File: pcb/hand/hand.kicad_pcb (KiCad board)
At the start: 2 copper layers, 172.5 x 135.2 mm, 48 parts, among them J1 Conn_01x15, J2 Conn_01x15

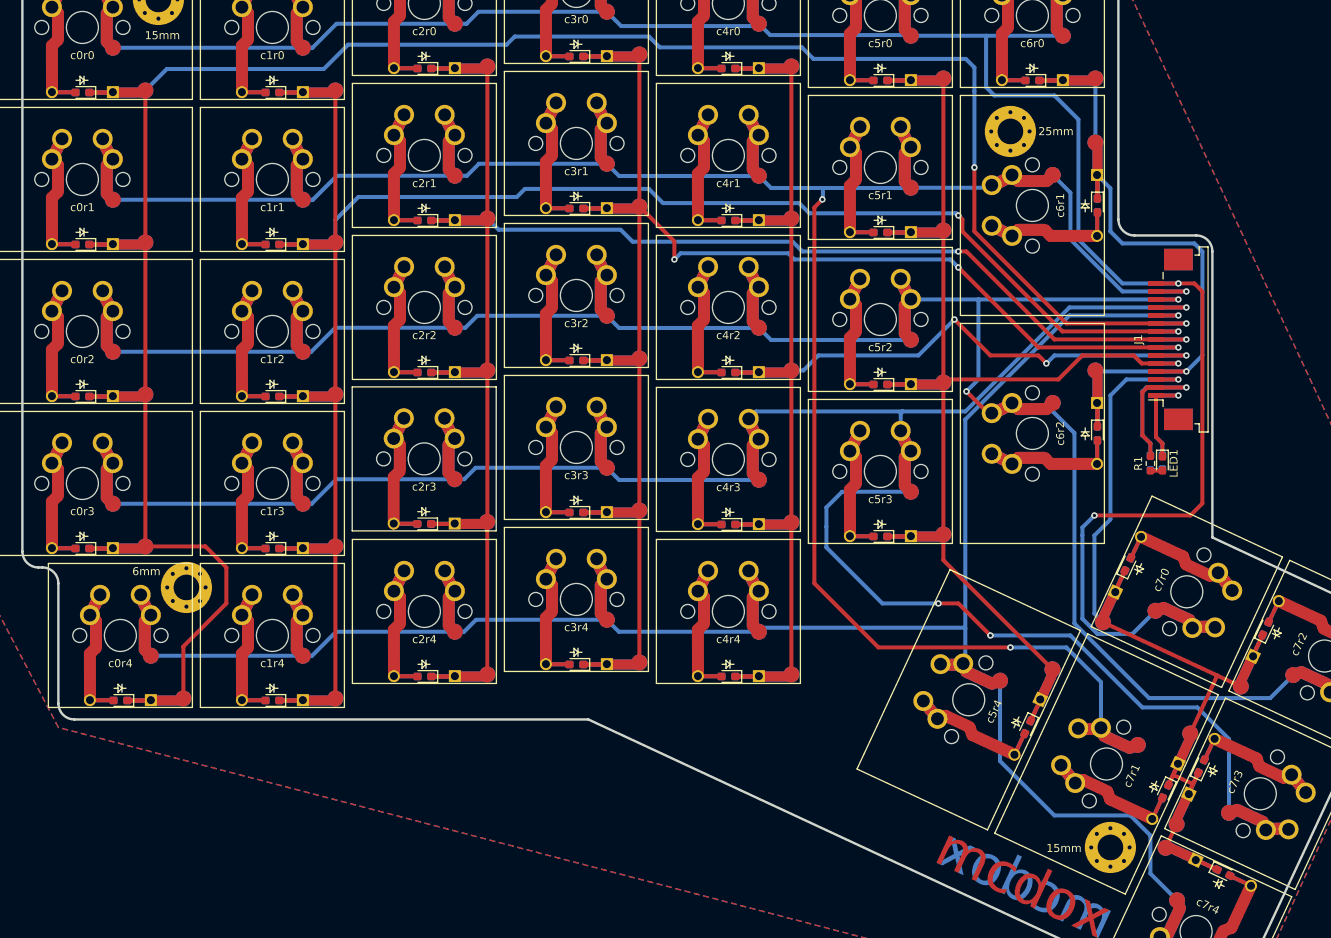
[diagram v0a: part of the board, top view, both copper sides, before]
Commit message: pcb/hand SOD123 diodes
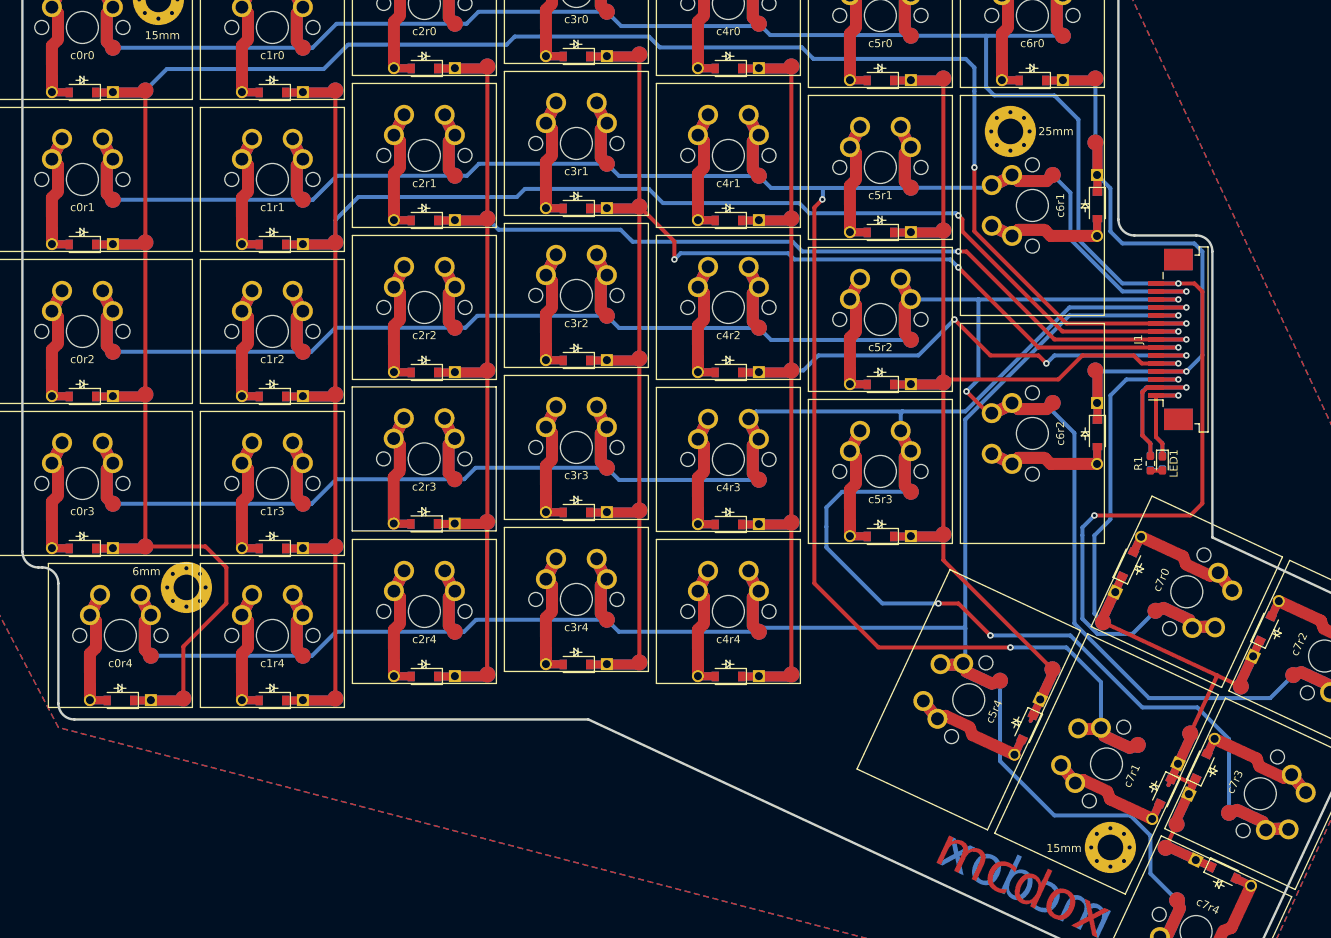
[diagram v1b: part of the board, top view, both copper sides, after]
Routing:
- net col7: track 145.9 -> 137.6 mm
- net col0: track 321.4 -> 313.4 mm
- net col2: track 244.5 -> 238.5 mm
- net col4: track 205.6 -> 199.6 mm
- net col3: track 226.5 -> 220.5 mm
- net col1: track 267.9 -> 261.9 mm
- net col6: track 102.0 -> 96.8 mm
- net col5: track 184.5 -> 179.7 mm

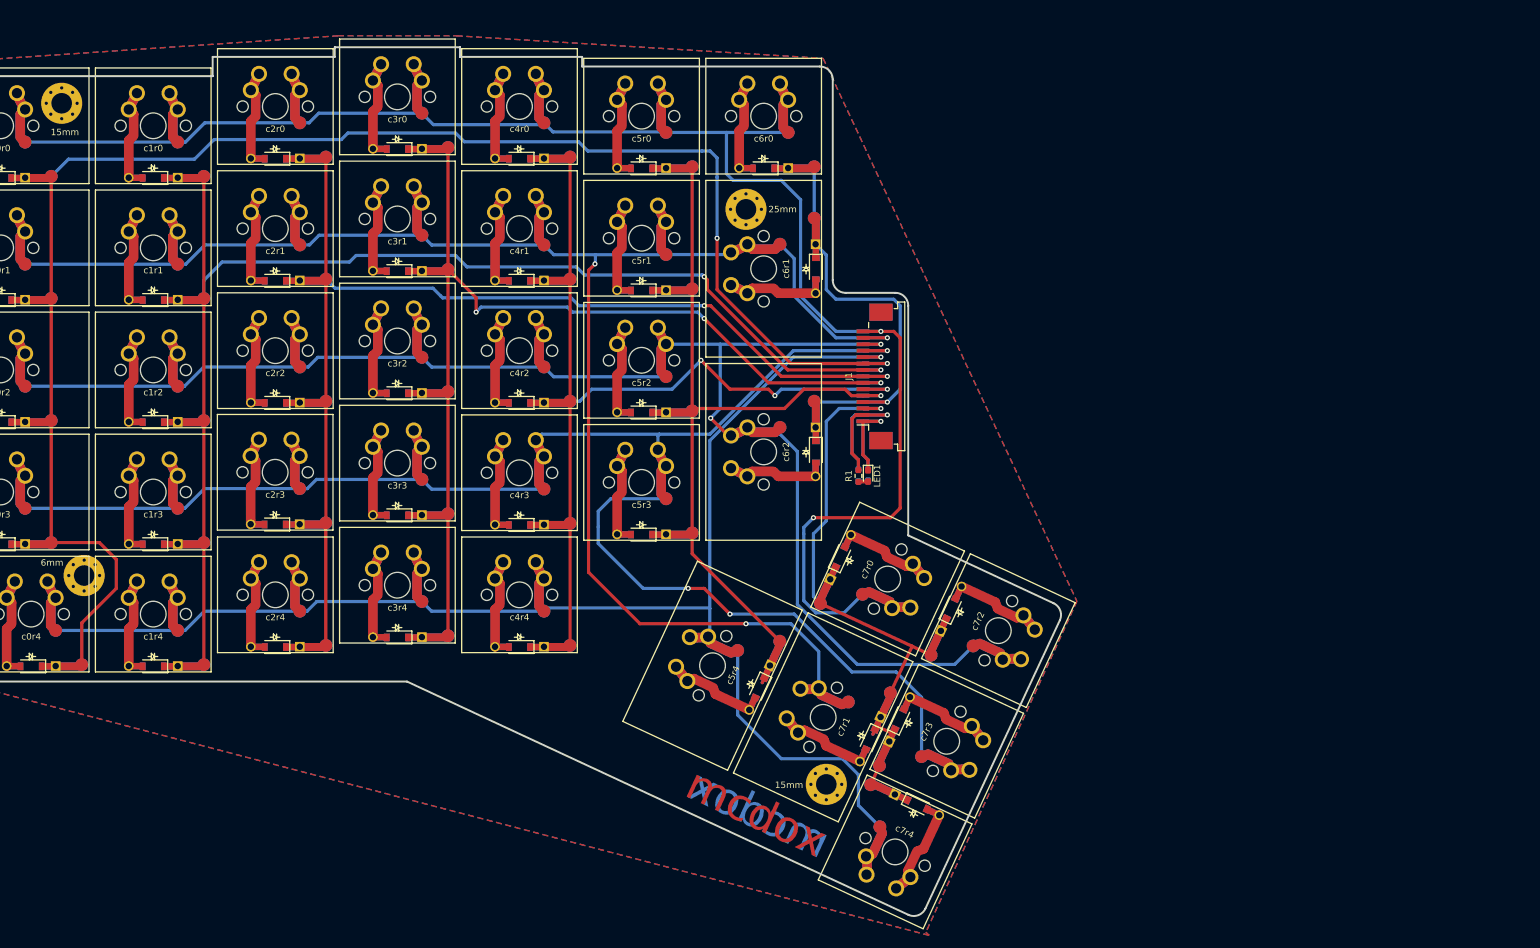
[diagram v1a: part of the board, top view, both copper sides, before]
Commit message: pcb/hand Thumb cluster rewired but not connected to rest of hand.
checkpoint
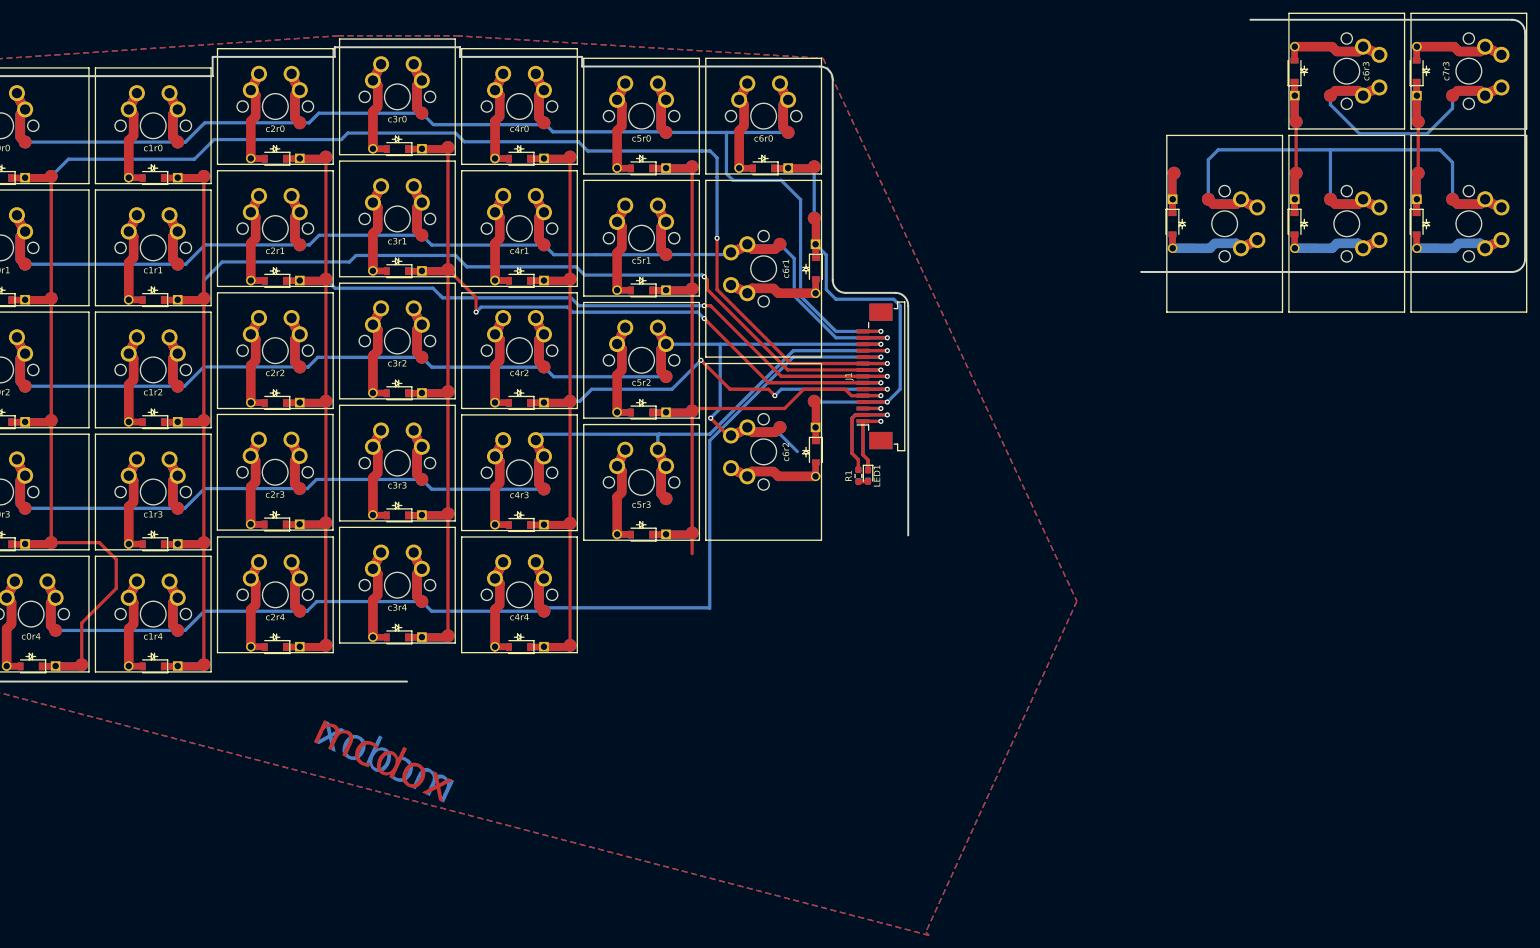
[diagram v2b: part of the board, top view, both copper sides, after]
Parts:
- removed 15mm (x2), 25mm, 6mm: MountingHole_3.2mm_M3_Pad_Via, MountingHole:MountingHole_3.2mm_M3_Pad_Via
- removed c7r0, c7r2: switchDiode, hand:reversibleMX_10u
- removed c7r1: switchDiode, hand:reversibleMX_15u
- added c6r3: switchDiode, hand:reversibleMX_10u, F.Cu at (253.5, 30.5)
- added c6r4: switchDiode, hand:reversibleMX_15u, B.Cu at (253.5, 54.2)
- c5r4: moved to B.Cu
- c7r4: footprint hand:reversibleMX_10u -> hand:reversibleMX_15u; moved to B.Cu
- moved c7r4 132.4 mm to (272.5, 54.2), turned to 90 degrees
- moved c7r3 132.2 mm to (272.5, 30.5), turned to 270 degrees
- moved c5r4 105.3 mm to (234.5, 54.2), turned to 90 degrees
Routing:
- net col7: track 137.6 -> 31.3 mm
- net row1: track 275.9 -> 174.9 mm, vias 3 -> 1
- net row0: track 285.7 -> 206.9 mm, vias 2 -> 1
- net row2: track 252.7 -> 191.9 mm
- net row3: track 267.9 -> 212.3 mm, vias 3 -> 1
- net col6: track 96.8 -> 123.1 mm
- net col5: track 179.7 -> 157.6 mm
- net row4: track 245.0 -> 261.1 mm
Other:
- board size 172.5 x 135.2 mm -> 244.8 x 103 mm

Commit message: pcb/hand Place thumb cluster at 30deg instead of 25, board outline.
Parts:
- moved c7r4 122.7 mm to (186.9, 142.1), turned to 60 degrees
- moved c7r3 117.2 mm to (198.8, 121.6), turned to 240 degrees
- moved c6r4 114.2 mm to (170.5, 132.6), turned to 60 degrees
- moved c6r3 108.2 mm to (182.3, 112.1), turned to 240 degrees
- moved c5r4 105.9 mm to (154.0, 123.1), turned to 60 degrees
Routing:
- net row3: track 212.3 -> 265.5 mm, vias 1 -> 3
- net col7: track 31.3 -> 73.9 mm
- net col6: track 123.1 -> 146.3 mm
- net row4: track 261.1 -> 271.5 mm
- net col5: track 157.6 -> 164.6 mm
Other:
- board size 244.8 x 103 mm -> 178.2 x 125.2 mm
